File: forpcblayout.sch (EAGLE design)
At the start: 76 parts, among them J1 3x2 M, J3 629105136821, SW2 !RESET, T1 2N2222, T2 2N2222, T3 2N2222, T4 2N2222, U3 ATMEGA32U4-AUR, X2 16 MHz

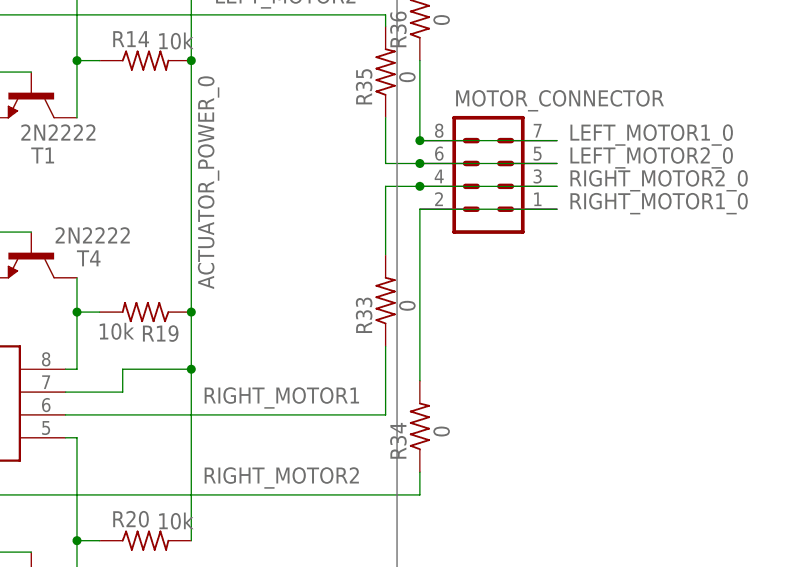
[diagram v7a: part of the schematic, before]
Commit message: De-de-fucked motor header connections
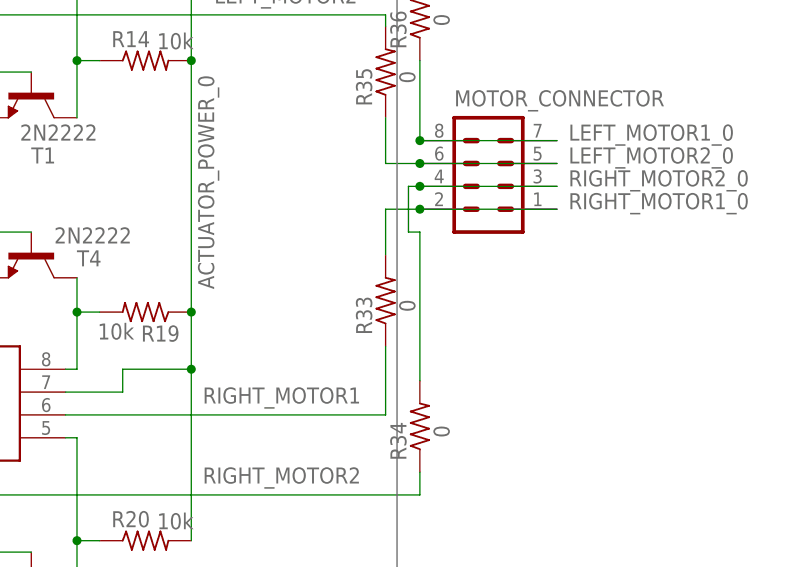
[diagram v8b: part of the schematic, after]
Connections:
- net RIGHT_MOTOR1_0: now also MOTOR_CONNECTOR.1, MOTOR_CONNECTOR.2; no longer MOTOR_CONNECTOR.3, MOTOR_CONNECTOR.4
- net RIGHT_MOTOR2_0: now also MOTOR_CONNECTOR.3, MOTOR_CONNECTOR.4; no longer MOTOR_CONNECTOR.1, MOTOR_CONNECTOR.2
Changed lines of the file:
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@@
 <segment>
 <pinref part="R33" gate="G$1" pin="2"/>
-<pinref part="MOTOR_CONNECTOR" gate="G$1" pin="4"/>
-<wire x1="508" y1="190.5" x2="508" y2="182.88" width="0.1524" layer="91"/>
-<wire x1="511.81" y1="190.5" x2="508" y2="190.5" width="0.1524" layer="91"/>
+<pinref part="MOTOR_CONNECTOR" gate="G$1" pin="2"/>
+<wire x1="508" y1="187.96" x2="508" y2="182.88" width="0.1524" layer="91"/>
+<wire x1="511.81" y1="187.96" x2="508" y2="187.96" width="0.1524" layer="91"/>
 <label x="528.32" y="187.96" size="1.778" layer="95"/>
-<pinref part="MOTOR_CONNECTOR" gate="G$1" pin="3"/>
-<wire x1="511.81" y1="190.5" x2="527.05" y2="190.5" width="0.1524" layer="91"/>
-<junction x="511.81" y="190.5"/>
+<pinref part="MOTOR_CONNECTOR" gate="G$1" pin="1"/>
+<wire x1="511.81" y1="187.96" x2="527.05" y2="187.96" width="0.1524" layer="91"/>
+<junction x="511.81" y="187.96"/>
 </segment>
 </net>
@@
 <net name="RIGHT_MOTOR2_0" class="0">
 <segment>
-<pinref part="MOTOR_CONNECTOR" gate="G$1" pin="2"/>
+<pinref part="MOTOR_CONNECTOR" gate="G$1" pin="4"/>
 <label x="528.32" y="190.5" size="1.778" layer="95"/>
-<pinref part="MOTOR_CONNECTOR" gate="G$1" pin="1"/>
-<wire x1="511.81" y1="187.96" x2="527.05" y2="187.96" width="0.1524" layer="91"/>
+<pinref part="MOTOR_CONNECTOR" gate="G$1" pin="3"/>
+<wire x1="511.81" y1="190.5" x2="527.05" y2="190.5" width="0.1524" layer="91"/>
+<wire x1="511.81" y1="190.5" x2="510.54" y2="190.5" width="0.1524" layer="91"/>
+<junction x="511.81" y="190.5"/>
+<wire x1="510.54" y1="190.5" x2="510.54" y2="185.42" width="0.1524" layer="91"/>
+<wire x1="510.54" y1="185.42" x2="511.81" y2="185.42" width="0.1524" layer="91"/>
 <pinref part="R34" gate="G$1" pin="2"/>
-<wire x1="511.81" y1="168.91" x2="511.81" y2="187.96" width="0.1524" layer="91"/>
+<wire x1="511.81" y1="185.42" x2="511.81" y2="168.91" width="0.1524" layer="91"/>
 </segment>
 </net>
